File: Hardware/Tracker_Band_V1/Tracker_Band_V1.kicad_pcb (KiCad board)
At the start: 2 copper layers, 10 parts, among them J1 USB_C_USB20, U1 ESP32-C3-MINI-1-N4, U2 BNO085, U3 RT8010, U4 MCP73832-2-AC, U5 LM66200

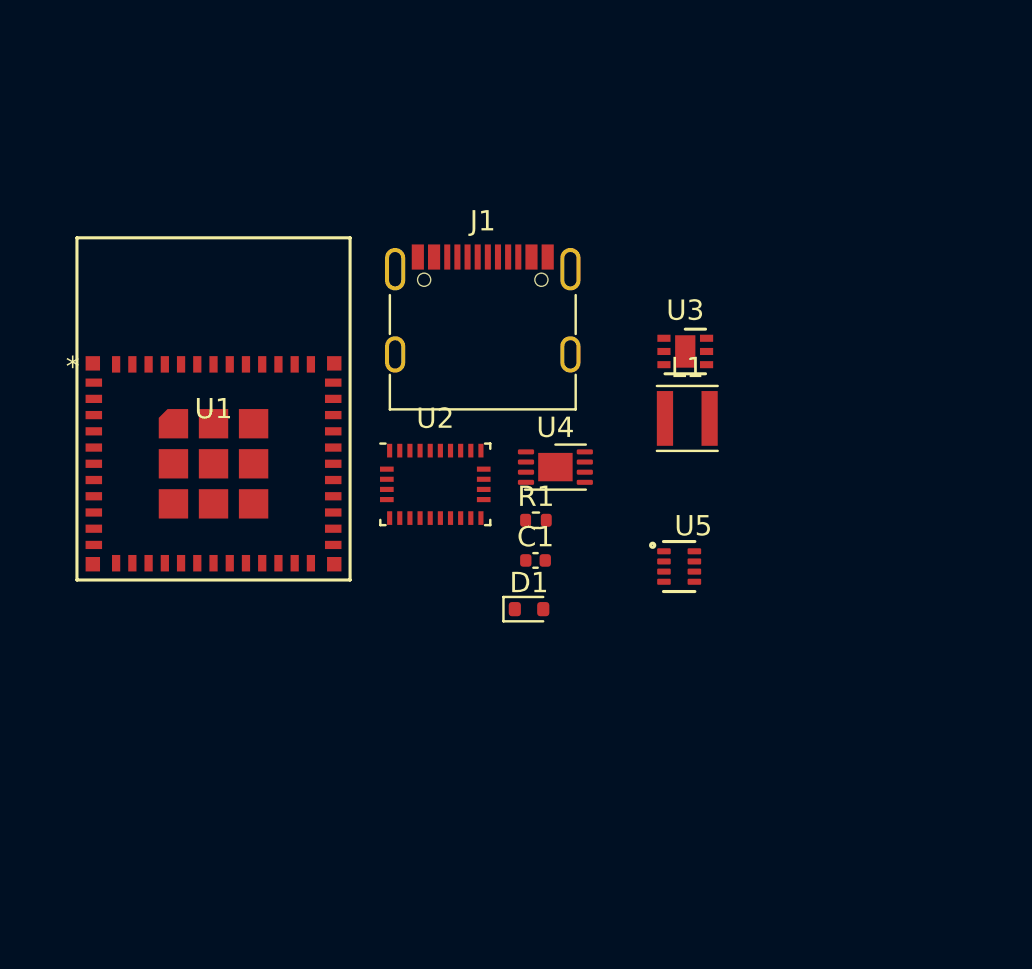
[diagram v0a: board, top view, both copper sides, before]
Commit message: Updated schematic wiring
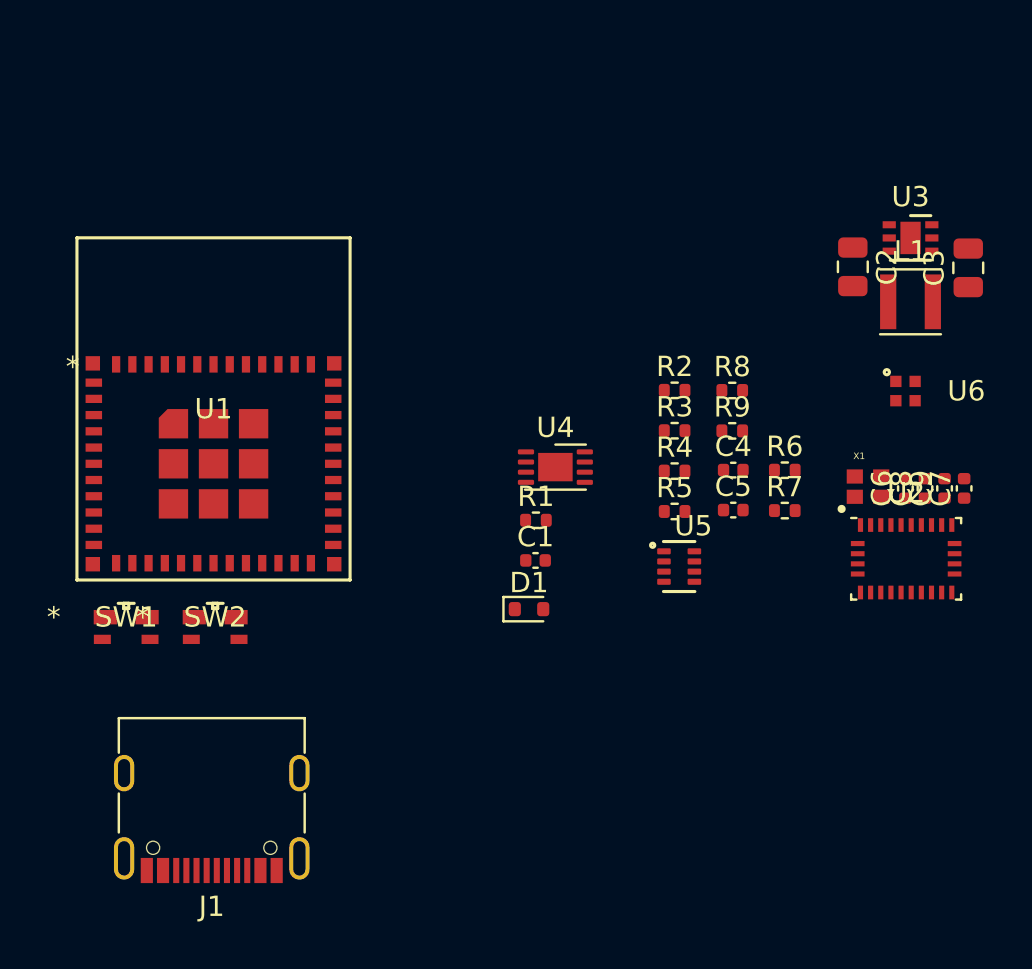
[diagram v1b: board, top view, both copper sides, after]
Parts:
- added C2: 10u, Capacitor_SMD:C_0805_2012Metric, F.Cu at (156.2, 81.1)
- added C3: 10u, Capacitor_SMD:C_0805_2012Metric, F.Cu at (161.8, 81.2)
- added C4: 1u, Capacitor_SMD:C_0402_1005Metric, F.Cu at (150.3, 91.1)
- added C5: 10u, Capacitor_SMD:C_0402_1005Metric, F.Cu at (150.3, 93.1)
- added C6: 100n, Capacitor_SMD:C_0402_1005Metric, F.Cu at (158.8, 92.0)
- added C7: 100n, Capacitor_SMD:C_0402_1005Metric, F.Cu at (161.6, 92.0)
- added C8: 100n, Capacitor_SMD:C_0402_1005Metric, F.Cu at (159.7, 92.0)
- added C9: 100n, Capacitor_SMD:C_0402_1005Metric, F.Cu at (160.7, 92.0)
- added R2: 100k, Resistor_SMD:R_0402_1005Metric, F.Cu at (147.4, 87.2)
- added R3: 100k, Resistor_SMD:R_0402_1005Metric, F.Cu at (147.4, 89.2)
- added R4: 10k, Resistor_SMD:R_0402_1005Metric, F.Cu at (147.4, 91.2)
- added R5: 100k, Resistor_SMD:R_0402_1005Metric, F.Cu at (147.4, 93.2)
- added R6: 100k, Resistor_SMD:R_0402_1005Metric, F.Cu at (152.8, 91.2)
- added R7: 5.1k, Resistor_SMD:R_0402_1005Metric, F.Cu at (152.8, 93.1)
- added R8: 5.1k, Resistor_SMD:R_0402_1005Metric, F.Cu at (150.2, 87.2)
- added R9: 0, Resistor_SMD:R_0402_1005Metric, F.Cu at (150.2, 89.2)
- added SW1: EVP-AVAA1A, 00_tracker_fp:EVP-AVAA1A_PAN, F.Cu at (120.3, 99.3)
- added SW2: EVP-AVAA1A, 00_tracker_fp:EVP-AVAA1A_PAN, F.Cu at (124.7, 99.3)
- added U6: IN-PI15TAT5R5G5B, 00_tracker_fp:IN-PI15_INL, F.Cu at (158.8, 87.3)
- added X1: 32.768kHz, 00_tracker_fp:OSC_ECS-1618-300-BN-TR, F.Cu at (156.9, 92.0)
- moved J1 26.4 mm to (124.6, 107.2), turned to 180 degrees
- moved U2 23.5 mm to (158.8, 95.5)
- moved U3 12.4 mm to (159.0, 79.7)
- moved L1 12.4 mm to (159.0, 82.9)
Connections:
- C1 pad 1: Net-(C1-Pad1) -> Net-(U1-EN)
- D1 pad 1: unconnected-(D1-K-Pad1) -> /BUCK_EN
- D1 pad 2: unconnected-(D1-A-Pad2) -> VBUS
- J1 pad A1: Net-(J1-GND-PadA1) -> GND
- J1 pad A12: Net-(J1-GND-PadA1) -> GND
- J1 pad A4: Net-(J1-VBUS-PadA4) -> VBUS
- J1 pad A5: unconnected-(J1-CC1-PadA5) -> Net-(J1-CC1)
- J1 pad A6: unconnected-(J1-D+-PadA6) -> /USB_D+
- J1 pad A7: unconnected-(J1-D--PadA7) -> /USB_D-
- J1 pad A9: Net-(J1-VBUS-PadA4) -> VBUS
- J1 pad B1: Net-(J1-GND-PadA1) -> GND
- J1 pad B12: Net-(J1-GND-PadA1) -> GND
- J1 pad B4: Net-(J1-VBUS-PadA4) -> VBUS
- J1 pad B5: unconnected-(J1-CC2-PadB5) -> Net-(J1-CC2)
- J1 pad B6: unconnected-(J1-D+-PadB6) -> /USB_D+
- J1 pad B7: unconnected-(J1-D--PadB7) -> /USB_D-
- J1 pad B9: Net-(J1-VBUS-PadA4) -> VBUS
- J1 pad S1: unconnected-(J1-SHIELD-PadS1) -> GND
- R1 pad 2: Net-(C1-Pad1) -> Net-(U1-EN)
- U1 pad 1: unconnected-(U1-GND-Pad1) -> GND
- U1 pad 11: unconnected-(U1-GND-Pad11) -> GND
- U1 pad 14: unconnected-(U1-GND-Pad14) -> GND
- U1 pad 2: unconnected-(U1-GND-Pad2) -> GND
- U1 pad 26: unconnected-(U1-IO18-Pad26) -> /USB_D-
- U1 pad 27: unconnected-(U1-IO19-Pad27) -> /USB_D+
- U1 pad 3: unconnected-(U1-3V3-Pad3) -> +3.3V
- U1 pad 36: unconnected-(U1-GND-Pad36) -> GND
- U1 pad 37: unconnected-(U1-GND-Pad37) -> GND
- U1 pad 38: unconnected-(U1-GND-Pad38) -> GND
- U1 pad 39: unconnected-(U1-GND-Pad39) -> GND
- U1 pad 40: unconnected-(U1-GND-Pad40) -> GND
- U1 pad 41: unconnected-(U1-GND-Pad41) -> GND
- U1 pad 42: unconnected-(U1-GND-Pad42) -> GND
- U1 pad 43: unconnected-(U1-GND-Pad43) -> GND
- U1 pad 44: unconnected-(U1-GND-Pad44) -> GND
- U1 pad 45: unconnected-(U1-GND-Pad45) -> GND
- U1 pad 46: unconnected-(U1-GND-Pad46) -> GND
- U1 pad 47: unconnected-(U1-GND-Pad47) -> GND
- U1 pad 48: unconnected-(U1-GND-Pad48) -> GND
- U1 pad 49: unconnected-(U1-GND-Pad49) -> GND
- U1 pad 50: unconnected-(U1-GND-Pad50) -> GND
- U1 pad 51: unconnected-(U1-GND-Pad51) -> GND
- U1 pad 52: unconnected-(U1-GND-Pad52) -> GND
- U1 pad 53: unconnected-(U1-GND-Pad53) -> GND
- U1 pad 54: unconnected-(U1-GND-Pad54) -> GND
- U1 pad 55: unconnected-(U1-GND-Pad55) -> GND
- U1 pad 56: unconnected-(U1-GND-Pad56) -> GND
- U1 pad 57: unconnected-(U1-GND-Pad57) -> GND
- U1 pad 58: unconnected-(U1-GND-Pad58) -> GND
- U1 pad 59: unconnected-(U1-GND-Pad59) -> GND
- U1 pad 60: unconnected-(U1-GND-Pad60) -> GND
- U1 pad 61: unconnected-(U1-GND-Pad61) -> GND
- U1 pad 8: unconnected-(U1-EN-Pad8) -> Net-(U1-EN)
- U2 pad 10: unconnected-(U2-CLKSEL0-Pad10) -> +3.3V
- U2 pad 11: unconnected-(U2-~{RST}-Pad11) -> /BNO_RSTn
- U2 pad 14: unconnected-(U2-~{H_INT}-Pad14) -> /BNO_INTn
- U2 pad 15: unconnected-(U2-S_SCL-Pad15) -> /BNO_SCL
- U2 pad 16: unconnected-(U2-S_SDA-Pad16) -> /BNO_SDA
- U2 pad 17: unconnected-(U2-SA0/MOSI-Pad17) -> /BNO_MOSI
- U2 pad 18: unconnected-(U2-~{H_CS}-Pad18) -> /BNO_CSn
- U2 pad 19: unconnected-(U2-H_SCL/SCLK/RX-Pad19) -> /BNO_SCLK
- U2 pad 2: unconnected-(U2-GND-Pad2) -> GND
- U2 pad 20: unconnected-(U2-H_SDA/MISO/TX-Pad20) -> /BNO_MISO
- U2 pad 25: unconnected-(U2-GNDIO-Pad25) -> GND
- U2 pad 26: unconnected-(U2-XOUT32/CLKSEL1-Pad26) -> Net-(U2-XOUT32/CLKSEL1)
- U2 pad 27: unconnected-(U2-XIN32-Pad27) -> Net-(U2-XIN32)
- U2 pad 28: unconnected-(U2-VDDIO-Pad28) -> +3.3V
- U2 pad 3: unconnected-(U2-VDD-Pad3) -> +3.3V
- U2 pad 4: unconnected-(U2-~{BOOT}-Pad4) -> +3.3V
- U2 pad 5: unconnected-(U2-PS1-Pad5) -> +3.3V
- U2 pad 6: unconnected-(U2-PS0/WAKE-Pad6) -> +3.3V
- U2 pad 9: unconnected-(U2-CAP-Pad9) -> Net-(U2-CAP)
- U3 pad 2: unconnected-(U3-EN-Pad2) -> /BUCK_EN
- U3 pad 3: unconnected-(U3-VIN-Pad3) -> Net-(U3-VIN)
- U4 pad 1: unconnected-(U4-V_{DD}-Pad1) -> VBUS
- U4 pad 2: unconnected-(U4-V_{DD}-Pad2) -> VBUS
- U4 pad 3: unconnected-(U4-V_{BAT}-Pad3) -> +BATT
- U4 pad 4: unconnected-(U4-V_{BAT}-Pad4) -> +BATT
- U4 pad 5: unconnected-(U4-STAT-Pad5) -> /CHRG_ST
- U4 pad 6: unconnected-(U4-V_{SS}-Pad6) -> GND
- U4 pad 8: unconnected-(U4-PROG-Pad8) -> Net-(U4-PROG)
- U5 pad 1: unconnected-(U5-GND-Pad1) -> GND
- U5 pad 2: unconnected-(U5-VOUT-Pad2) -> Net-(U3-VIN)
- U5 pad 3: unconnected-(U5-VIN1-Pad3) -> +BATT
- U5 pad 4: unconnected-(U5-~{ON}-Pad4) -> Net-(U5-~{ON})
- U5 pad 5: unconnected-(U5-GND-Pad5) -> GND
- U5 pad 6: unconnected-(U5-VIN2-Pad6) -> VBUS
- U5 pad 7: unconnected-(U5-VOUT-Pad7) -> Net-(U3-VIN)
- U5 pad 8: unconnected-(U5-ST-Pad8) -> /OR_ST

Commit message: started layout
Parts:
- added C10: 100n, Capacitor_SMD:C_0402_1005Metric, F.Cu at (131.7, 92.5)
- added C11: 100n, Capacitor_SMD:C_0402_1005Metric, F.Cu at (139.8, 88.0)
- added D2: 1N4148WT, Diode_SMD:D_SOD-523, F.Cu at (124.0, 83.4)
- added D3: GREEN, LED_SMD:LED_0603_1608Metric, F.Cu at (131.8, 95.5)
- added D4: 1N4148WT, Diode_SMD:D_SOD-523, F.Cu at (140.1, 83.4)
- added Q1: SSM6L56FE, Package_TO_SOT_SMD:SOT-563, F.Cu at (131.3, 88.8)
- added R10: 100k, Resistor_SMD:R_0402_1005Metric, F.Cu at (128.5, 88.9)
- added R11: 100k, Resistor_SMD:R_0402_1005Metric, F.Cu at (131.7, 91.4)
- added R12: 120k, Resistor_SMD:R_0402_1005Metric, F.Cu at (131.7, 90.4)
- added R13: 22, Resistor_SMD:R_0402_1005Metric, F.Cu at (131.8, 97.0)
- added R14: 22, Resistor_SMD:R_0402_1005Metric, F.Cu at (131.8, 98.0)
- added R15: 10k, Resistor_SMD:R_0402_1005Metric, F.Cu at (124.0, 92.7)
- added R16: 10k, Resistor_SMD:R_0402_1005Metric, F.Cu at (128.5, 87.9)
- added R17: 1k, Resistor_SMD:R_0402_1005Metric, F.Cu at (124.0, 79.2)
- added R18: 2.2k, Resistor_SMD:R_0402_1005Metric, F.Cu at (131.8, 94.2)
- added R19: 100k, Resistor_SMD:R_0402_1005Metric, F.Cu at (124.0, 80.3)
- added R20: 100k, Resistor_SMD:R_0402_1005Metric, F.Cu at (124.0, 81.3)
- added R21: 1k, Resistor_SMD:R_0402_1005Metric, F.Cu at (131.8, 99.1)
- added R22: 100k, Resistor_SMD:R_0402_1005Metric, F.Cu at (140.1, 81.3)
- added U7: IN-PI15TAT5R5G5B, 00_tracker_fp:IN-PI15_INL, F.Cu at (140.2, 77.0)
- added U8: IN-PI15TAT5R5G5B, 00_tracker_fp:IN-PI15_INL, F.Cu at (124.0, 86.1)
- added U9: IN-PI15TAT5R5G5B, 00_tracker_fp:IN-PI15_INL, F.Cu at (140.2, 86.1)
- C4: value 1u -> 10u; footprint Capacitor_SMD:C_0402_1005Metric -> Capacitor_SMD:C_0805_2012Metric
- C5: footprint Capacitor_SMD:C_0402_1005Metric -> Capacitor_SMD:C_0805_2012Metric
- R6: value 100k -> 4.7k
- moved C7 37.7 mm to (124.0, 94.8), turned to 180 degrees
- moved C9 36.8 mm to (124.0, 95.8), turned to 180 degrees
- moved U6 36.3 mm to (124.0, 77.0)
- moved C8 36.0 mm to (124.0, 96.8), turned to 180 degrees
- moved C6 35.2 mm to (124.0, 97.8), turned to 180 degrees
- moved X1 33.8 mm to (124.0, 99.7), turned to 90 degrees
- moved U2 31.4 mm to (127.5, 97.8), turned to 90 degrees
- moved R6 28.4 mm to (126.5, 101.9)
- moved R9 26.6 mm to (124.0, 93.8)
- moved C3 23.9 mm to (139.9, 90.6)
- moved C2 23.9 mm to (134.2, 90.6)
- moved L1 23.9 mm to (137.1, 92.3)
- moved U3 23.9 mm to (137.1, 89.1)
- moved R7 22.4 mm to (131.8, 101.1)
- moved R8 22.4 mm to (131.8, 100.1)
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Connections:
- net Net-(U3-VIN) renamed VCC
- D1 pad 2: VBUS -> Net-(D1-A)
- J1 pad A6: /USB_D+ -> Net-(J1-D+-PadA6)
- J1 pad A7: /USB_D- -> Net-(J1-D--PadA7)
- J1 pad B6: /USB_D+ -> Net-(J1-D+-PadA6)
- J1 pad B7: /USB_D- -> Net-(J1-D--PadA7)
- SW1 pad 1: unconnected-(SW1-Pad1) -> Net-(R17-Pad2)
- SW1 pad 4: unconnected-(SW1-A-Pad4) -> Net-(D2-A)
- SW2 pad 1: unconnected-(SW2-Pad1) -> GND
- SW2 pad 4: unconnected-(SW2-A-Pad4) -> /SW_2
- U6 pad 1: unconnected-(U6-DIN-Pad1) -> /RGB_LED
- U6 pad 2: unconnected-(U6-VDD-Pad2) -> +3.3V
- U6 pad 3: unconnected-(U6-DOUT-Pad3) -> Net-(U6-DOUT)
- U6 pad 4: unconnected-(U6-GND-Pad4) -> GND
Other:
- board outline added: 18.5 x 30 mm
- copper layers 2 -> 4

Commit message: Component positioning & PCB sizing
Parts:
- removed R4: 10k, Resistor_SMD:R_0402_1005Metric
- R22: value 100k -> 1k
- moved SW2 24.1 mm to (122.8, 79.5)
- moved SW1 19.9 mm to (140.6, 79.5), turned to 90 degrees
- moved R17 18.9 mm to (139.9, 89.4)
- moved C1 17.3 mm to (123.4, 83.7), turned to 180 degrees
- moved R1 17.2 mm to (123.4, 84.7)
- moved R19 16.0 mm to (139.9, 82.0)
- moved R20 16.0 mm to (139.9, 83.0)
- moved D2 16.0 mm to (139.9, 84.2), turned to 180 degrees
- moved C11 14.7 mm to (125.8, 92.7), turned to 180 degrees
- moved C10 12.8 mm to (123.4, 82.8), turned to 180 degrees
- moved R12 12.0 mm to (123.4, 81.8), turned to 180 degrees
- moved R7 11.9 mm to (136.7, 90.2), turned to 180 degrees
- moved C5 11.4 mm to (133.1, 92.8), turned to 90 degrees
- moved R3 10.8 mm to (136.6, 88.1), turned to -90 degrees
- moved C3 9.85 mm to (130.4, 88.1), turned to 180 degrees
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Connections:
- net Net-(U6-DOUT) renamed /RGB_LED1
- net Net-(U7-DOUT) renamed /RGB_LED2
- net Net-(U8-DOUT) renamed /RGB_LED3
- R17 pad 2: Net-(R17-Pad2) -> Net-(SW1-A)
- SW1 pad 1: Net-(R17-Pad2) -> Net-(D2-A)
- SW1 pad 2: unconnected-(SW1-Pad2) -> Net-(D2-A)
- SW1 pad 4: Net-(D2-A) -> Net-(SW1-A)
- U1 pad 6: unconnected-(U1-GPIO3,_ADC1_CH3-Pad6) -> /VBAT_ADC
- U3 pad 7: (no net) -> GND
- U4 pad 9: (no net) -> GND
- U5 pad 4: Net-(U5-~{ON}) -> GND
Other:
- board size 18.5 x 30 mm -> 19.2 x 25.8 mm

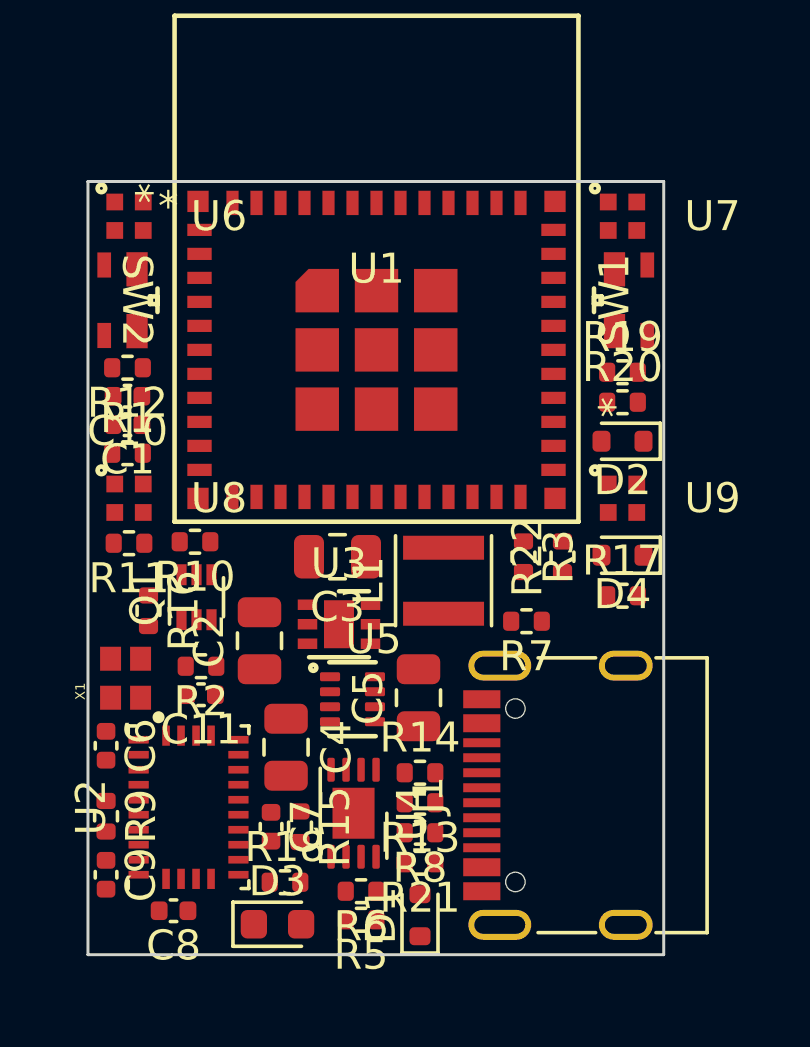
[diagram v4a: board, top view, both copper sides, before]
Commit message: Started layout
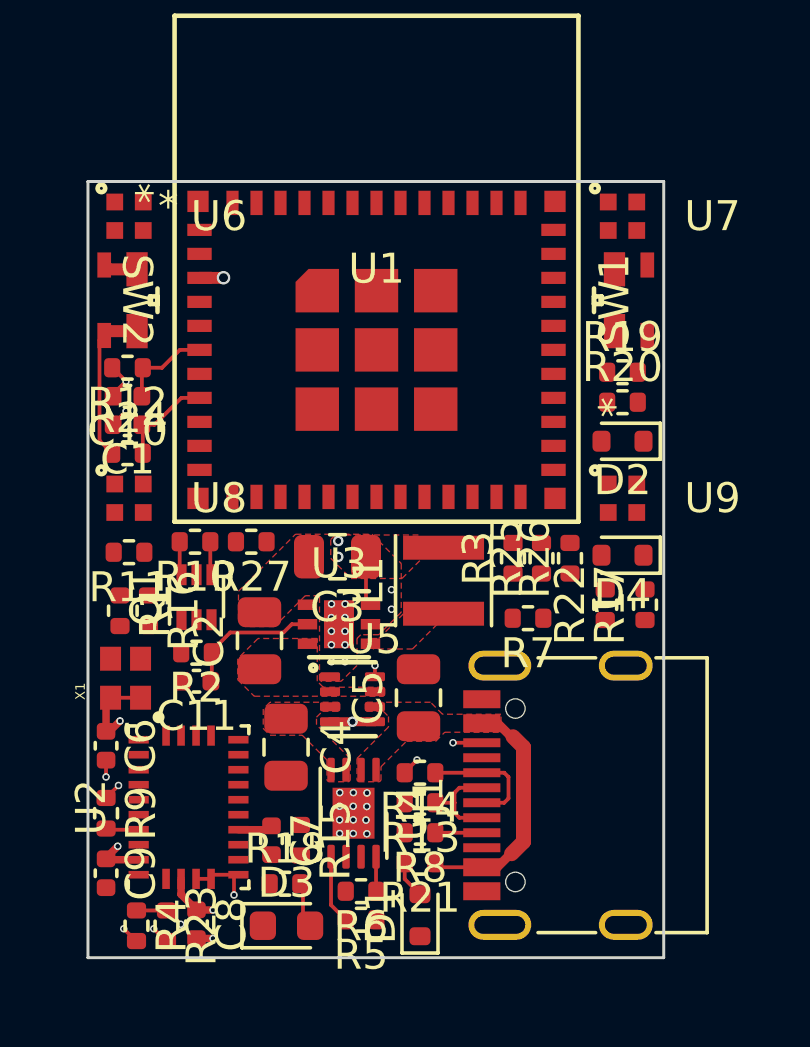
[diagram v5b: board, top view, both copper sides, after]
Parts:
- added R23: 2.2k, Resistor_SMD:R_0402_1005Metric, F.Cu at (124.7, 100.4)
- added R24: 0, Resistor_SMD:R_0402_1005Metric, F.Cu at (123.4, 84.7)
- added R25: 10k, Resistor_SMD:R_0402_1005Metric, F.Cu at (137.2, 88.2)
- added R26: 10k, Resistor_SMD:R_0402_1005Metric, F.Cu at (138.2, 88.2)
- added R27: 10k, Resistor_SMD:R_0402_1005Metric, F.Cu at (127.5, 87.6)
- added R4: 2.2k, Resistor_SMD:R_0402_1005Metric, F.Cu at (123.7, 100.4)
- R17: value 1k -> 470
- R19, R3, R5: value 100k -> 10k
- moved R1 5.26 mm to (123.2, 89.9), turned to -90 degrees
- moved R22 2.14 mm to (139.3, 89.7)
- moved C8 0.89 mm to (125.7, 100.3), turned to -90 degrees
- moved R17 0.81 mm to (140.7, 89.7), turned to 90 degrees
- moved C11 0.47 mm to (125.7, 92.2)
- moved R2 0.47 mm to (125.7, 91.3)
- moved C7 0.45 mm to (128.2, 97.5)
- moved R15 0.45 mm to (129.2, 97.5)
- moved R3 0.35 mm to (136.2, 88.2), turned to 90 degrees
- moved D3 0.30 mm to (128.7, 100.4)
- moved R11 0.30 mm to (123.5, 88.0)
- moved R7 0.11 mm to (136.8, 90.2)
- moved R9 0.10 mm to (122.7, 96.7)
- turned R14 to 180 degrees
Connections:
- net Net-(D2-A) renamed /BUCK_EN_SW
- net Net-(U1-EN) renamed /RST_N
- net Net-(U3-LX) renamed /LX
- R22 pad 1: Net-(D4-A) -> /BUCK_EN_MCU
- R22 pad 2: unconnected-(R22-Pad2) -> Net-(D4-A)
- SW2 pad 2: unconnected-(SW2-Pad2) -> GND
- SW2 pad 3: unconnected-(SW2-K-Pad3) -> /SW_2
- U1 pad 22: unconnected-(U1-GPIO8-Pad22) -> Net-(U1-GPIO8)
- U1 pad 23: unconnected-(U1-GPIO9-Pad23) -> Net-(U1-GPIO9)
- U1 pad 5: unconnected-(U1-GPIO2,_ADC1_CH2,_FSPIQ-Pad5) -> Net-(U1-GPIO2,_ADC1_CH2,_FSPIQ)
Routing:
- net +3.3V: track 0.00 -> 12.8 mm, vias 0 -> 9
- net VBUS: track 0.00 -> 8.43 mm
- net GND: track 0.00 -> 5.76 mm, vias 0 -> 29
- net /SW_2: track 0.00 -> 5.32 mm
- net /BUCK_EN: track 0.00 -> 4.58 mm
- net Net-(J1-D+-PadA6): track 0.00 -> 4.16 mm
- net Net-(J1-D--PadA7): track 0.00 -> 3.27 mm
- net /RST_N: track 0.00 -> 3.25 mm
- net /VBAT_ADC: track 0.00 -> 3.10 mm
- net /CHRG_ST: track 0.00 -> 2.30 mm
- net Net-(Q1A-D): track 0.00 -> 1.62 mm
- net Net-(J1-CC1): track 0.00 -> 1.55 mm
- net Net-(D3-A): track 0.00 -> 1.54 mm
- net Net-(D1-A): track 0.00 -> 1.26 mm
- net Net-(U2-CAP): track 0.00 -> 1.16 mm
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- added copper zone on F.Cu, net +3.3V
- added copper zone on F.Cu, net +BATT
- added copper zone on F.Cu, net /LX
- added copper zone on F.Cu, net GND
- added copper zone on F.Cu, net VBUS
- added copper zone on F.Cu, net VCC
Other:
- board size 19.2 x 25.8 mm -> 19.2 x 25.9 mm
